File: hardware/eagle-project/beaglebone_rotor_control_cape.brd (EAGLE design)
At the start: 71.8 x 54.6 mm, 62 parts, among them IC1 TLC2264CDU, IC2 MCP4901, IC3 MAX3232ESE, IC4 TLC2264CDU, IC5 MCP4901, IC6 TLC2264CDU, Q1 SQ2348ES-T1-GE3, Q2 SQ2348ES-T1-GE3, Q3 SQ2348ES-T1-GE3, Q4 SQ2348ES-T1-GE3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

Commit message: Added DCDC to eagle schematic and made first draft of layout
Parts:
- removed C4, C5, C6, C8: 100n, rcl:C0603
- removed IC3: MAX3232ESE, maxim:SO16
- removed IC4: TLC2264CDU, ti-tlc2264cd:SO14
- removed IC5: MCP4901, microchip_mcp4901:SO-08
- removed R1, R14, R22, R23, R24, R25, R8: 100, rcl:R0805
- removed R15: 0, rcl:R0805
- removed R16: 5k, rcl:R0805
- removed R17: 10k, rcl:R0805
- removed X2, X3: DSUB9, con-te-dsub:DSUB9
- added Q6: SQ2348ES-T1-GE3, vishay_sq2348eS-t1-ge3:SOT23
- added R35: 1M, rcl:R0805
- added R36: 100, rcl:R0805
- added R37, R38, R39, R40: 10k, rcl:R0805
- added U1: TMH0512S, traco_dcdc:SIP
- added X4: DSUB9, con-te-dsub:DSUB9
- moved R33 383.5 mm to (63.5, 12.0), turned to 270 degrees
- moved R34 378.7 mm to (63.5, 8.50), turned to 180 degrees
- moved Q5 375.8 mm to (69.0, 9.50)
- moved R28 359.5 mm to (36.0, 41.0), turned to 270 degrees
- moved R32 359.4 mm to (51.0, 9.50), turned to 90 degrees
- moved D3 357.8 mm to (36.0, 45.5), turned to 180 degrees
- moved R29 354.7 mm to (48.5, 11.5), turned to 270 degrees
- moved R27 352.0 mm to (22.5, 34.5), turned to 90 degrees
- moved D4 351.6 mm to (33.0, 41.0)
- moved R30 350.1 mm to (39.0, 9.50), turned to 90 degrees
- moved R31 349.6 mm to (41.5, 9.50), turned to 90 degrees
- moved C9 349.1 mm to (26.5, 33.0)
- moved Q4 345.5 mm to (35.5, 11.5), turned to 90 degrees
- moved IC6 345.0 mm to (26.5, 42.0), turned to 90 degrees
- moved R26 344.4 mm to (26.0, 35.5)
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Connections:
- removed net BB_UART4_RX: R1.1, X1.57
- removed net BB_UART4_TX: R8.1, X1.59
- removed net N$16: C1.1, IC3.4
- removed net N$17: C1.2, IC3.5
- removed net N$18: C3.2, IC3.3
- removed net N$19: C3.1, IC3.1
- removed net N$20: C4.1, IC3.6
- removed net N$21: C5.1, IC3.2
- removed net N$22: IC3.11, R8.2
- removed net N$24: R34.1
- removed net N$25: IC3.12, R1.2
- removed net N$27: IC5.4, R23.2
- removed net N$28: IC5.3, R24.2
- removed net N$29: IC5.2, R25.2
- removed net N$30: R22.1
- removed net N$31: IC4.3, IC5.8
- removed net N$32: IC4.1, R14.1, R16.2
- removed net N$33: IC4.2, R16.1, R17.2
- removed net N$4: IC5.5, R15.2, R22.2
- removed net ROT_E_SPEED: R14.2
- removed net RS232_RX: IC3.13
- removed net RS232_TX: IC3.14
- removed net V+: IC6.4
- removed net V-: IC6.11
- new net +12V: R39.2, R40.2, U1.6
- new net ELEVATION_ROTOR_INTERFACE_SUPPLY: R36.1, X1.45
- new net N$34: Q6.1, R35.2, R36.2
- new net N$37: Q6.3, U1.2
- new net ROTOR_AC_SUPPLY: R34.1, X1.3
- net +3V3: no longer C6.1, C8.1, IC3.16, IC5.1, IC5.6
- net +5V: now also C1.1, C3.1, IC6.4, R37.2, R38.2, U1.1; no longer IC4.4
- net BB_SPI1_CS0: no longer R25.1
- net BB_SPI1_D0: no longer R23.1
- net BB_SPI1_SCLK: no longer R24.1
- net GND: now also C1.2, C3.2, IC6.11, Q6.2, R35.1, U1.4, X4.6; no longer C4.2, C5.2, C6.2, C8.2, IC3.15, IC4.11, IC5.7, R15.1, R17.1
- net ROT_E_DOWN: now also R37.1, R40.1
- net ROT_E_POSITION: now also X4.1; no longer X3.1
- net ROT_E_UP: now also R38.1, R39.1
- net ROT_H_LEFT: now also X4.3; no longer X3.3
- net ROT_H_POSITON: now also X4.5; no longer X3.5
- net ROT_H_RIGHT: now also X4.2; no longer X3.2
- net ROT_H_SPEED: now also X4.4; no longer X3.4
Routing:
- net +5V: track 25.8 -> 204.9 mm, vias 2 -> 7
- net BB_AIN_H: track 5.11 -> 45.7 mm, vias 0 -> 2
- net BB_AIN_E: track 0.00 -> 23.9 mm
- net +12V: track 0.00 -> 23.3 mm, vias 0 -> 2
- net N$35: track 0.00 -> 21.3 mm, vias 0 -> 2
- net ROT_E_POSITION: track 0.00 -> 16.4 mm, vias 0 -> 1
- net BB_DOUT_RIGHT: track 18.4 -> 2.90 mm
- net GND: track 15.1 -> 0.00 mm, vias 2 -> 21
- net N$37: track 0.00 -> 13.4 mm
- net N$36: track 0.00 -> 9.90 mm
- net BB_SPI0_CS0: track 0.00 -> 9.05 mm
- net BB_DOUT_DOWN: track 0.00 -> 8.83 mm
- net BB_SPI0_D0: track 0.00 -> 8.51 mm
- net N$23: track 0.00 -> 8.46 mm
- net N$14: track 0.00 -> 7.83 mm
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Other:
- board size 71.8 x 54.6 mm -> 83.8 x 62.6 mm

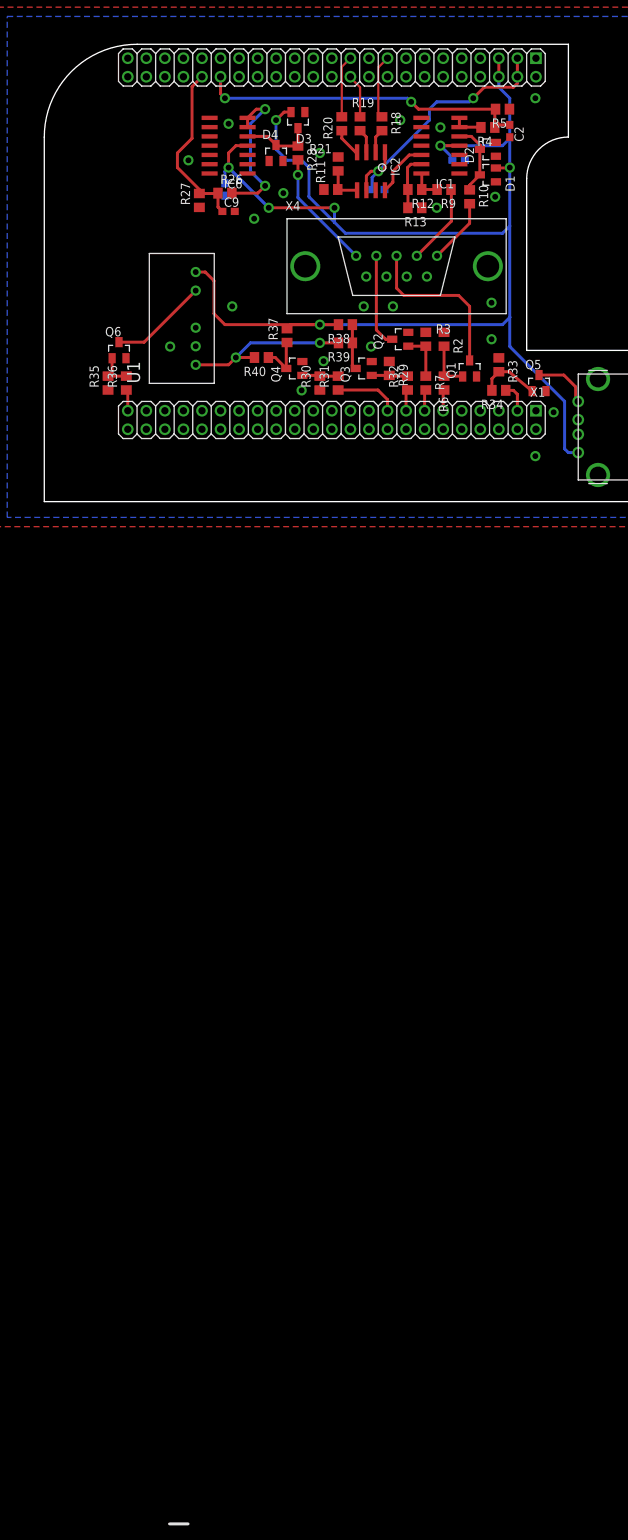
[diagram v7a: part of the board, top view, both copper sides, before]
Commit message: Improved Eagle layout, more free space on board for future components
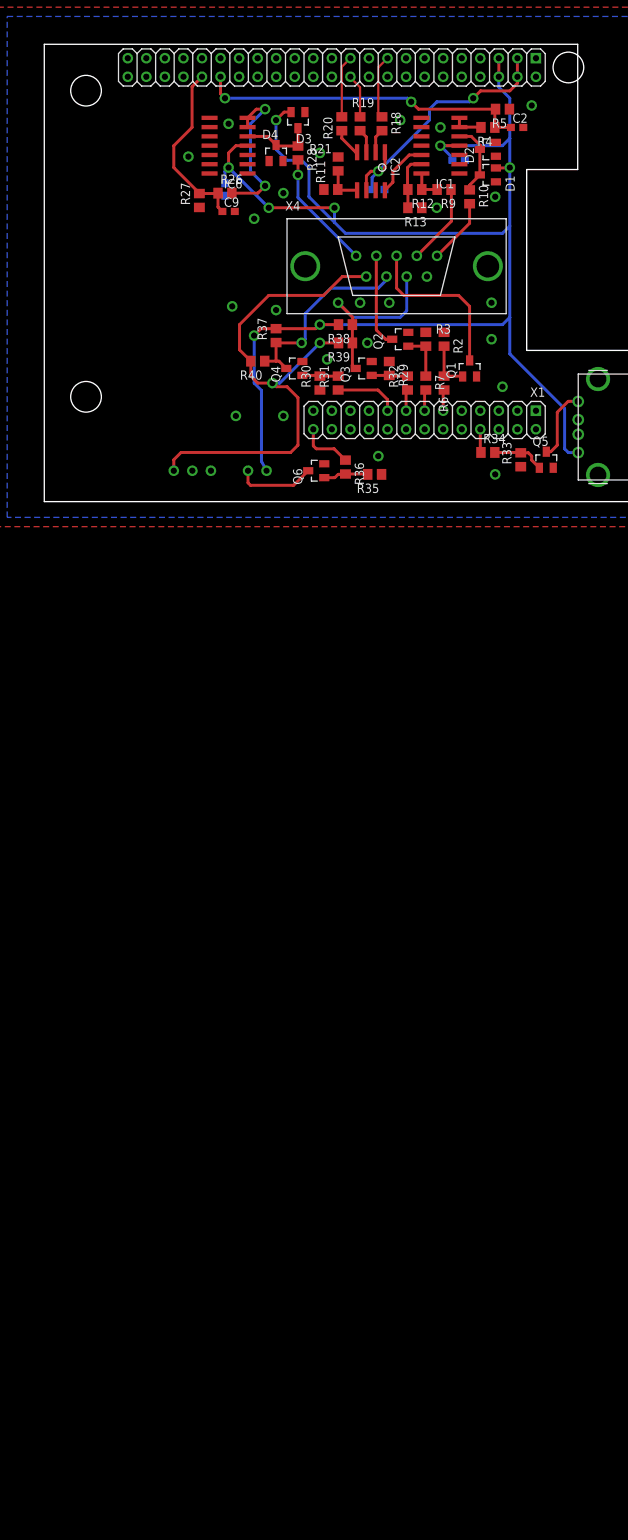
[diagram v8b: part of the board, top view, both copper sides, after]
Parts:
- moved R35 38.6 mm to (46.5, -3.00), turned to 180 degrees
- moved R36 32.1 mm to (42.5, -2.00), turned to 270 degrees
- moved Q6 31.6 mm to (38.5, -2.50), turned to 90 degrees
- moved U1 14.8 mm to (19.0, -2.50), flipped to the bottom, turned to 180 degrees
- moved R33 13.3 mm to (66.5, -1.00), turned to 90 degrees
- moved Q5 10.5 mm to (70.0, -1.00)
- moved R34 8.63 mm to (62.0, 0.00), turned to 0 degrees
- moved R37 1.50 mm to (33.0, 16.0)
- moved C2 1.12 mm to (66.0, 44.5), turned to 0 degrees
- moved R40 0.71 mm to (30.5, 12.5)
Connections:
- net BB_USB_VCC renamed N$4243
- net +12V: now also X4.6
- net ELEVATION_ROTOR_INTERFACE_SUPPLY: now also X1.26; no longer X1.45
- net GND: now also X1.80, X4.9; no longer X4.6
- net ROTOR_AC_SUPPLY: now also X1.8; no longer X1.3
- net ROT_E_DOWN: now also X4.7
- net ROT_E_UP: now also X4.8
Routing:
- net +12V: track 23.3 -> 72.6 mm
- net ROT_E_DOWN: track 6.66 -> 27.1 mm, vias 0 -> 1
- net ROT_E_UP: track 6.19 -> 25.3 mm, vias 0 -> 1
- net ELEVATION_ROTOR_INTERFACE_SUPPLY: track 2.92 -> 7.48 mm
- net N$37: track 13.4 -> 10.9 mm
- net N$14: track 7.83 -> 9.87 mm
- net +5V: track 204.9 -> 206.3 mm, vias 7 -> 8
- net N$23: track 8.46 -> 7.29 mm
- net N$34: track 5.18 -> 6.18 mm
- net ROTOR_AC_SUPPLY: track 4.06 -> 3.21 mm
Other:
- outline, holes or cut-outs redrawn
